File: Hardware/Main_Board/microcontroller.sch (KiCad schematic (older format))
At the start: 56 parts

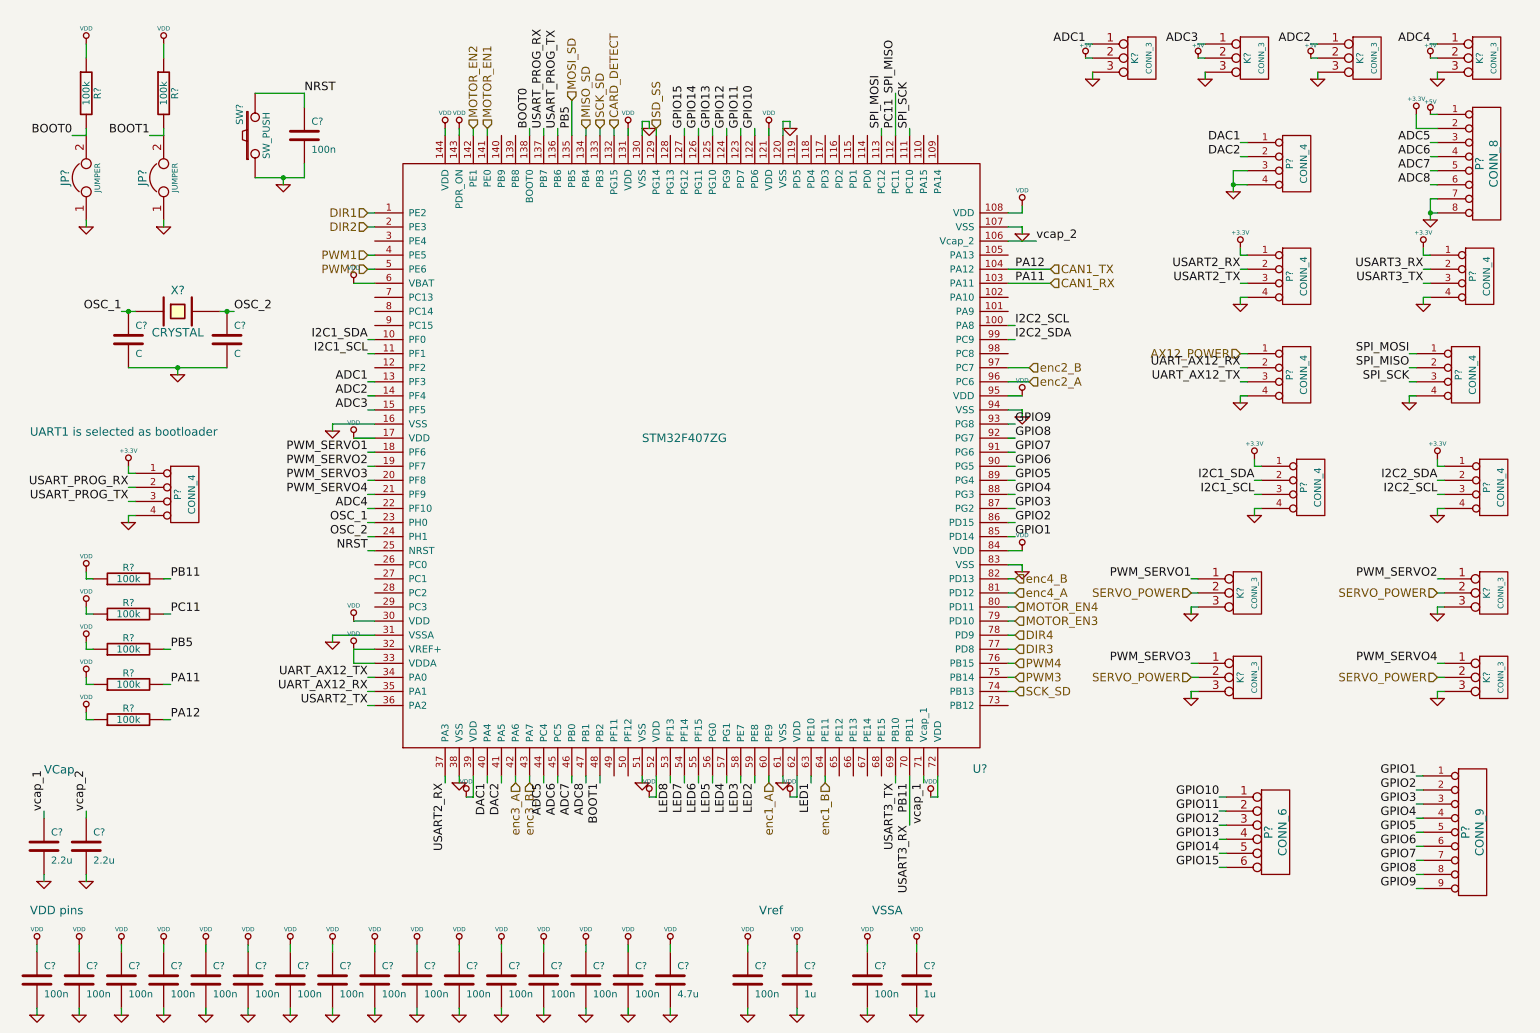
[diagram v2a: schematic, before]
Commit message: [HARDWARE] Add 4 ADC
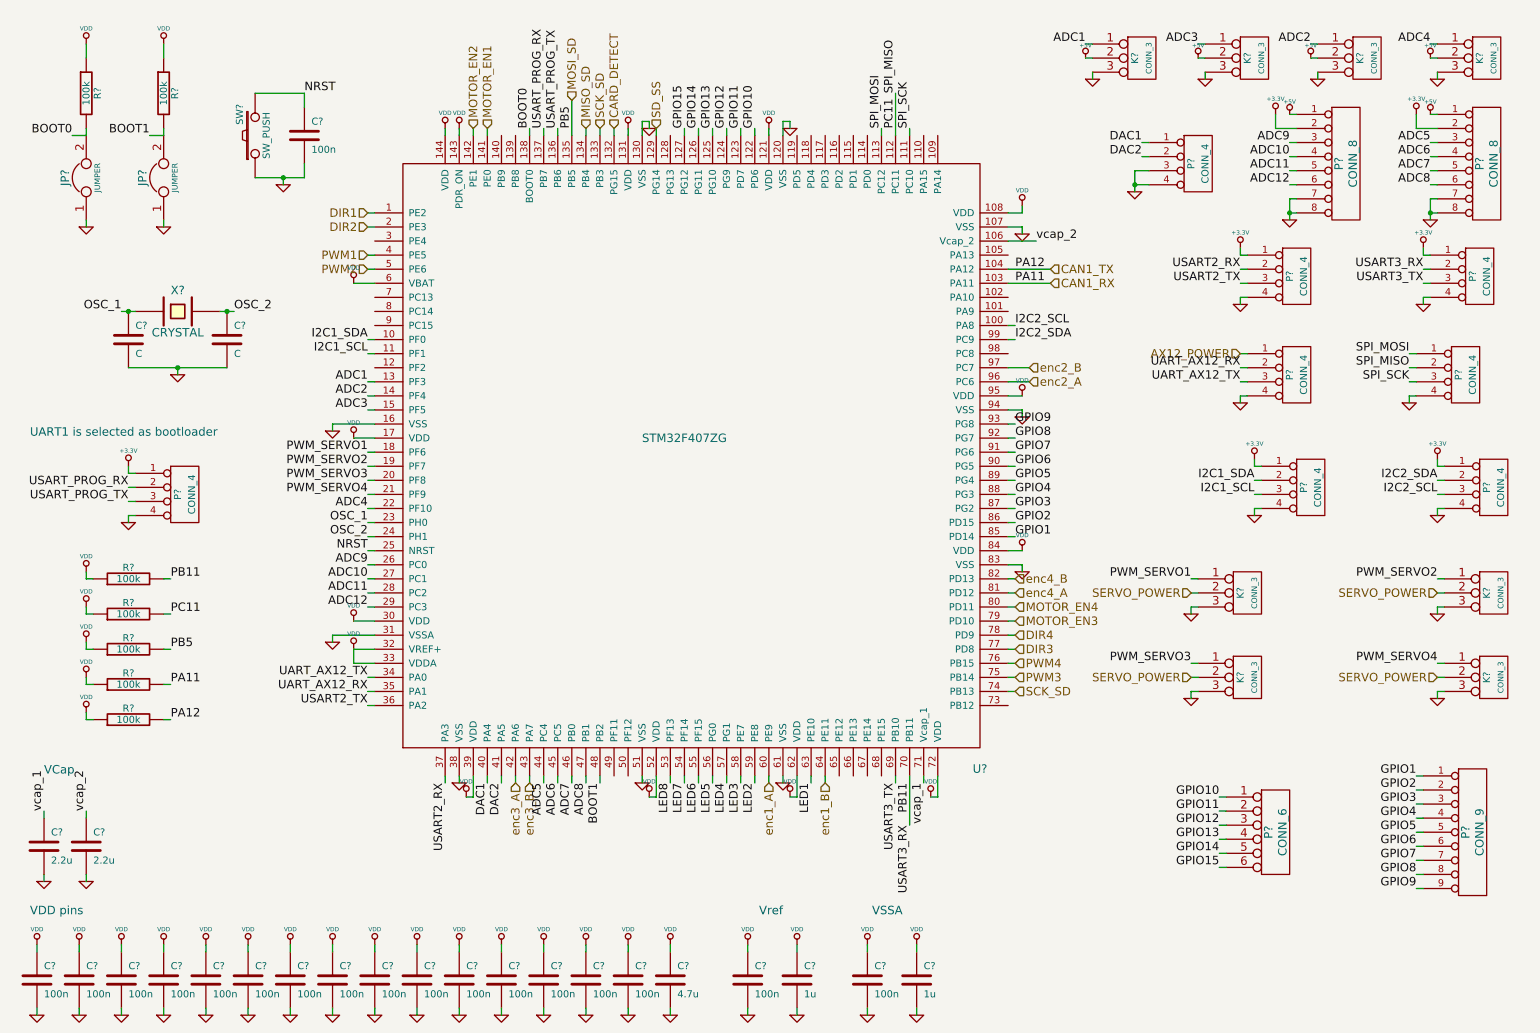
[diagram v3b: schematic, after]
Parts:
- added P?: CONN_8, symbol CONN_8
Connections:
- net +3.3V: now also P?.2 (P2)
- net +5V: now also P?.1 (P1)
- net GND: now also P?.7 (P7), P?.8 (P8)
- net ADC9: now reaches U?.26 (PC0)
- net ADC9: now also P?.3 (P3)
- net ADC10: now reaches U?.27 (PC1)
- net ADC10: now also P?.4 (P4)
- net ADC11: now reaches U?.28 (PC2)
- net ADC11: now also P?.5 (P5)
- net ADC12: now reaches U?.29 (PC3)
- net ADC12: now also P?.6 (P6)
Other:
- moved on the sheet: P?

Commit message: [HARDWARE] Finish motor interface and add SWD interface
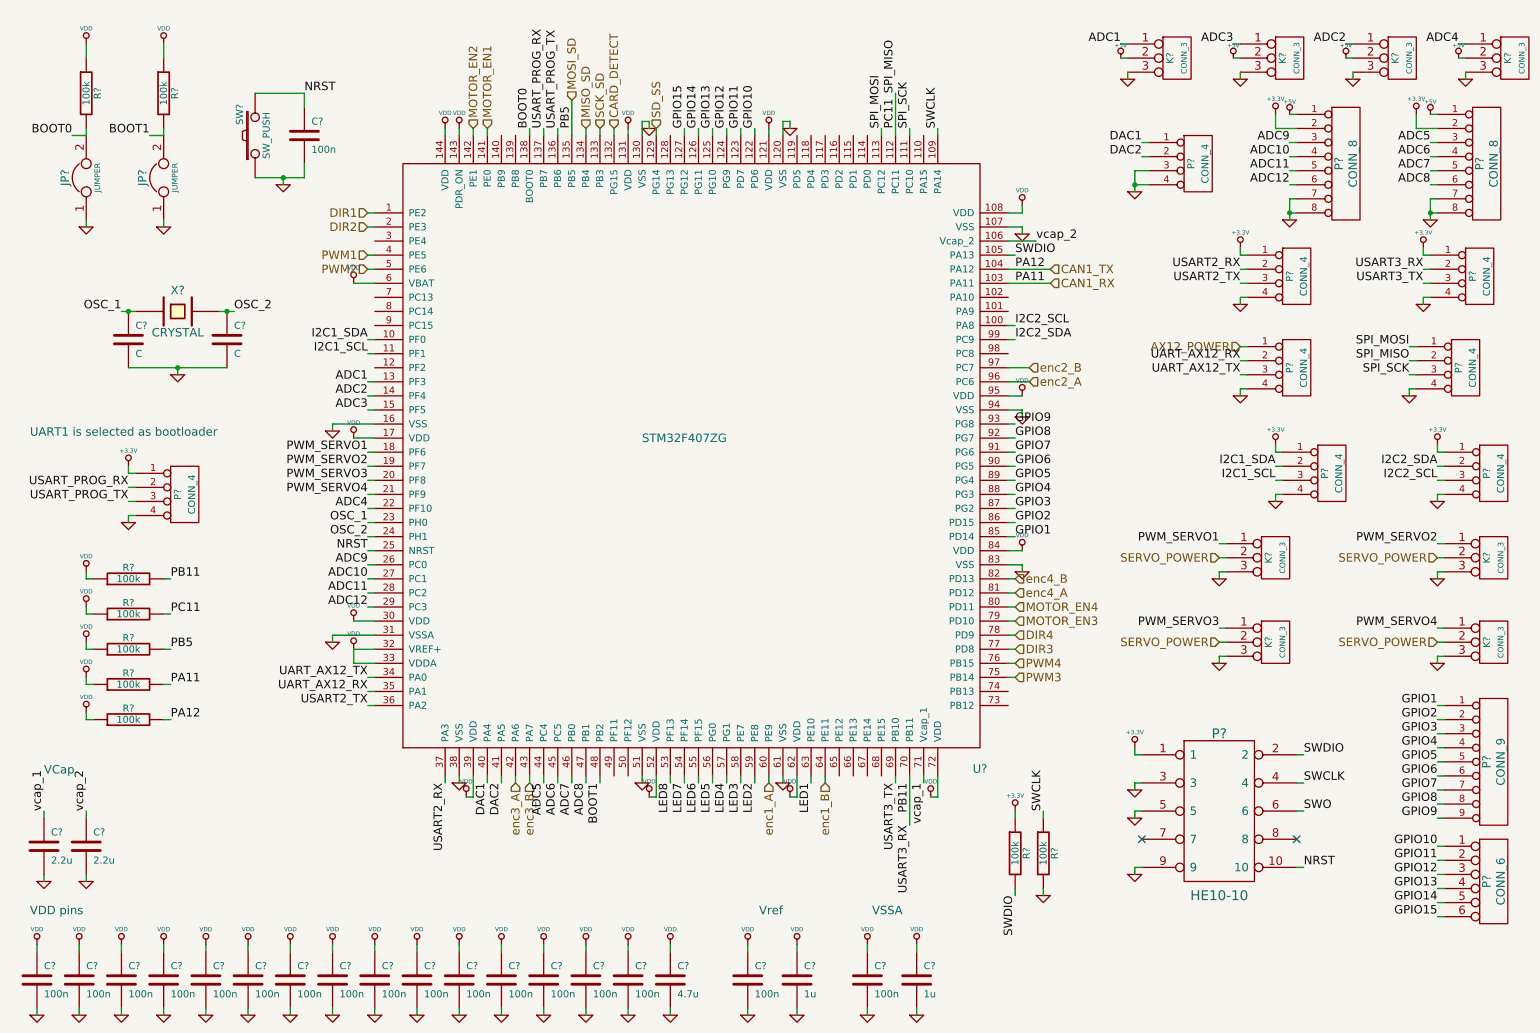
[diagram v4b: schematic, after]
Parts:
- added P?: HE10-10, symbol HE10-10
- added R? (x2): 100k, symbol R
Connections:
- net +3.3V: now also P?.1, R?.1
- net GND: now also P?.3, P?.5, P?.9, R?.2
- net NRST: now also P?.10
- net SCK_SD: no longer U?.74 (PB13)
- net SWDIO: now reaches U?.105 (PA13)
- net SWDIO: now also P?.2, R?.2
- net SWCLK: now reaches U?.109 (PA14)
- net SWCLK: now also P?.4, R?.1
- new net SWO: P?.6
- no-connect marks 0 -> 2
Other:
- moved on the sheet: K?, P?

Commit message: [HARDWARE] Complete the SWD design, remove two undrived motor interfaces
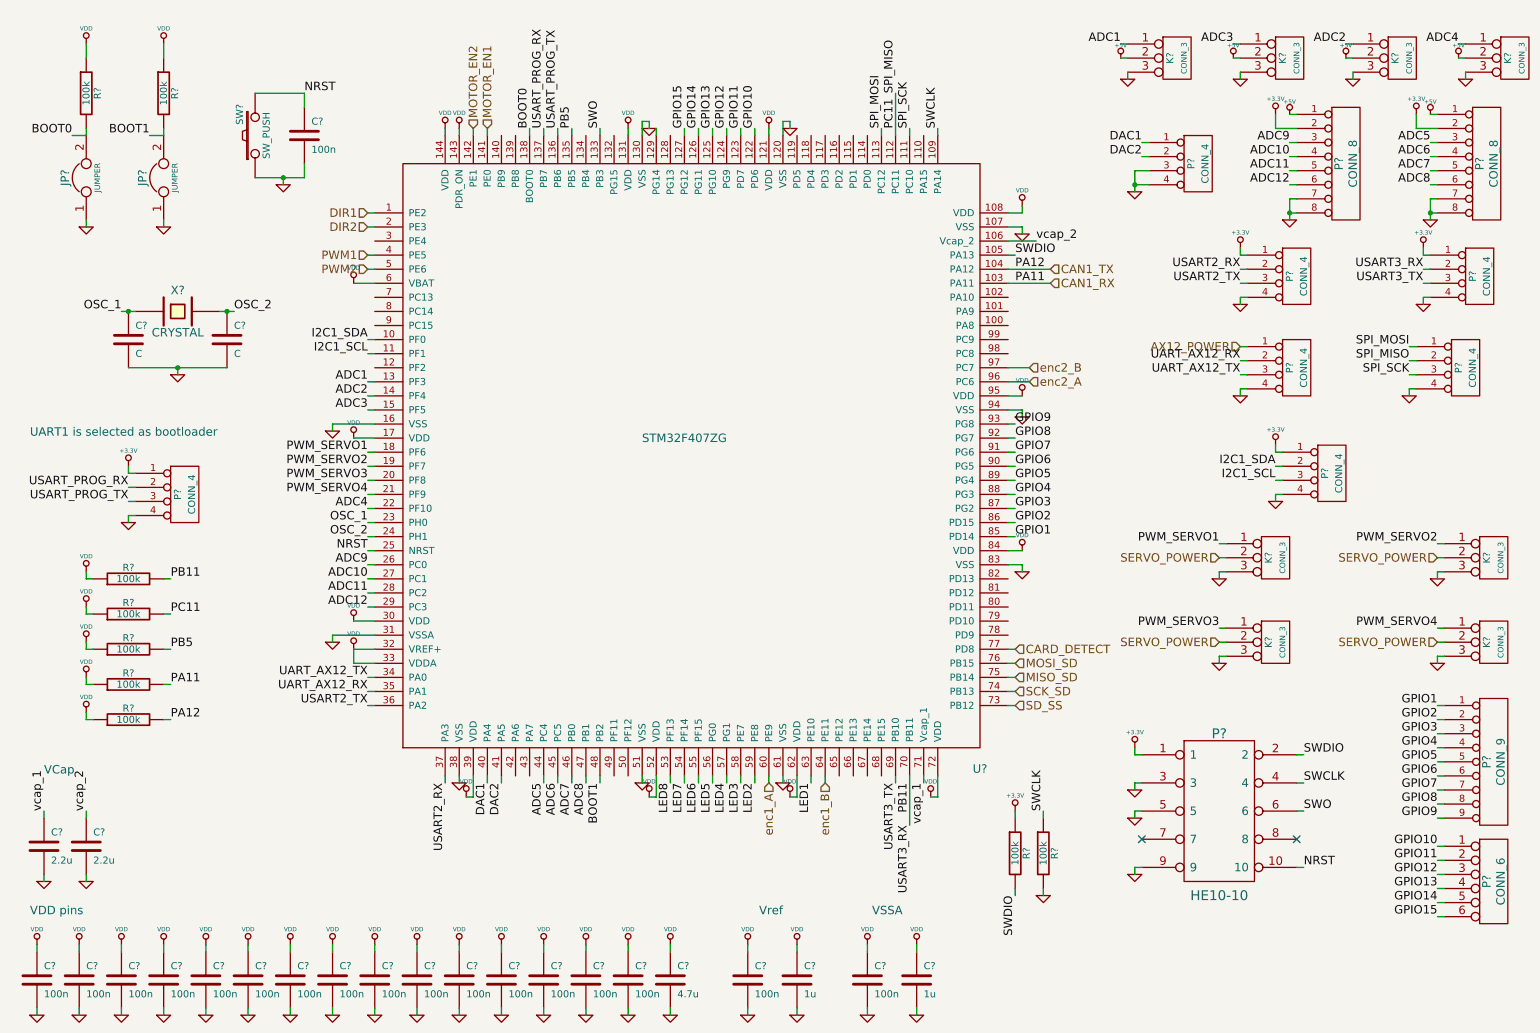
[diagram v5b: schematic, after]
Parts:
- removed P?: CONN_4, symbol CONN_4
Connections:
- net DIR3 is gone; now on net CARD_DETECT: U?.77 (PD8)
- net PWM3 is gone; now on net MISO_SD: U?.75 (PB14)
- net PWM4 is gone; now on net MOSI_SD: U?.76 (PB15)
- net CARD_DETECT: no longer U?.132 (PG15)
- net MISO_SD: no longer U?.134 (PB4)
- net MOSI_SD: no longer R?.2, U?.135 (PB5)
- net SCK_SD: now also U?.74 (PB13); no longer U?.133 (PB3)
- net SD_SS: now also U?.73 (PB12); no longer U?.129 (PG14)
- net SWO: now also U?.133 (PB3)
- net DIR4: no longer names the net of U?.78 (PD9)
- net I2C2_SCL: no longer names the net of U?.100 (PA8)
- net I2C2_SDA: no longer names the net of U?.99 (PC9)
- net MOTOR_EN3: no longer names the net of U?.79 (PD10)
- net MOTOR_EN4: no longer names the net of U?.80 (PD11)
- net enc3_A: no longer names the net of U?.42 (PA6)
- net enc3_B: no longer names the net of U?.43 (PA7)
- net enc4_A: no longer names the net of U?.81 (PD12)
- net enc4_B: no longer names the net of U?.82 (PD13)
- new net PB5: R?.2, U?.135 (PB5)

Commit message: [HARDWARE] Component association + schematic modifications
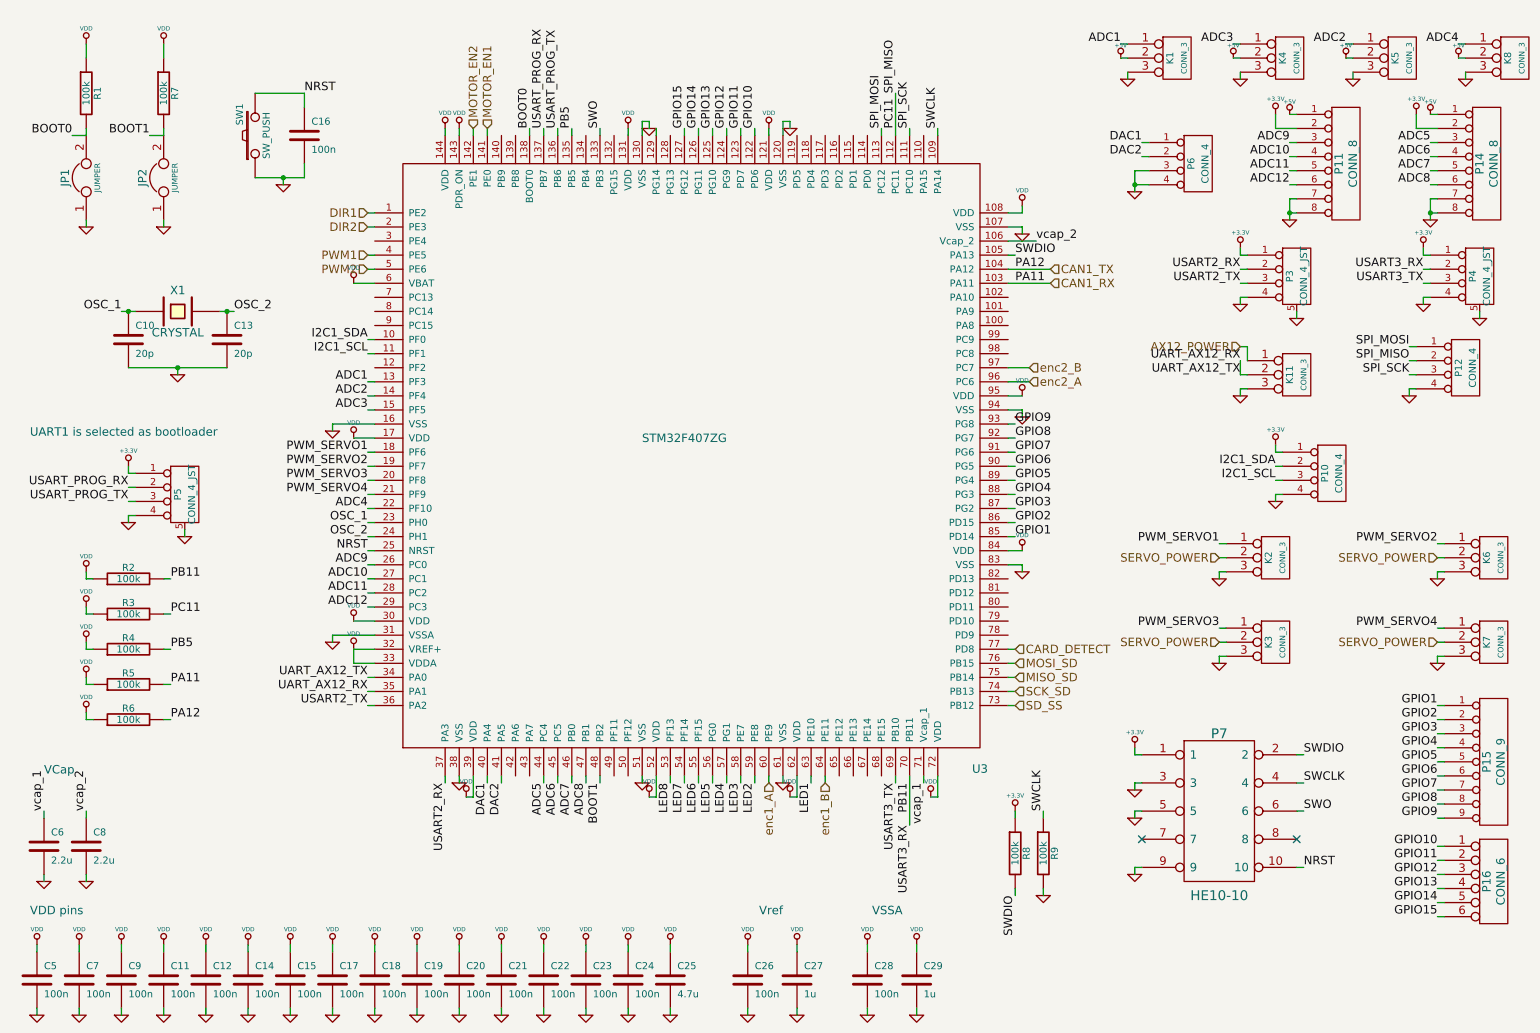
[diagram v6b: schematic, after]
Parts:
- removed P? (x4): CONN_4, symbol CONN_4
- added K11: CONN_3, symbol CONN_3
- added P3, P4, P5: CONN_4_JST, symbol CONN_4_JST
- C10, C13: renamed from C?; value C -> 20p
- gave numbers to parts that had none: 53
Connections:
- net UART_AX12_TX is gone; now on net UART_AX12_RX: U3.34 (PA0)
- net +3.3V: now also P3.1 (P1), P4.1 (P1), P5.1 (P1)
- net AX12_POWER: now also K11.1 (P1)
- net GND: now also K11.3 (P3), P3.4 (P4), P3.5 (Shield), P4.4 (P4), P4.5 (Shield), P5.4 (P4), P5.5 (Shield)
- net PB11: now also P4.2 (P2)
- net UART_AX12_RX: now also K11.2 (PM)
- net USART2_RX: now also P3.2 (P2)
- net USART2_TX: now also P3.3 (P3)
- net USART3_TX: now also P4.3 (P3)
- net USART_PROG_RX: now also P5.2 (P2)
- net USART_PROG_TX: now also P5.3 (P3)

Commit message: [HARDWARE] Update schematic and start routing
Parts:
- removed C23, C24, C28: 100n, symbol C
- removed C25: 4.7u, symbol C
- removed C29: 1u, symbol C
- removed P11: CONN_8, symbol CONN_8
- removed P16: CONN_6, symbol CONN_6
- added D10, D11, D12, D13, D14, D15, D16, D9: LED, symbol LED
- added R12, R13, R14, R15, R16, R17, R18, R19: 390, symbol R
- added R21, R22: 4.7k, symbol R
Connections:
- net GPIO10 is gone; now on net LED1: U3.122 (PD6)
- net GPIO11 is gone; now on net LED2: U3.123 (PD7)
- net GPIO12 is gone; now on net LED3: U3.124 (PG9)
- net GPIO13 is gone; now on net LED4: U3.125 (PG10)
- net GPIO14 is gone; now on net LED5: U3.126 (PG11)
- net GPIO15 is gone; now on net LED6: U3.127 (PG12)
- net +3.3V: now also R21.1, R22.1
- net CARD_DETECT: now also U3.68 (PE15); no longer U3.77 (PD8)
- net GND: now also D10.2 (K), D11.2 (K), D12.2 (K), D13.2 (K), D14.2 (K), D15.2 (K), D16.2 (K), D9.2 (K)
- net I2C1_SCL: now also R22.2
- net I2C1_SDA: now also R21.2
- net LED1: now also R12.1; no longer U3.63 (PE10)
- net LED2: now also R13.1; no longer U3.59 (PE8)
- net LED3: now also R14.1; no longer U3.58 (PE7)
- net LED4: now also R15.1; no longer U3.57 (PG1)
- net LED5: now also R16.1; no longer U3.56 (PG0)
- net LED6: now also R17.1; no longer U3.55 (PF15)
- net LED7: now also U3.128 (PG13), R18.1; no longer U3.54 (PF14)
- net LED8: now also U3.129 (PG14), R19.1; no longer U3.53 (PF13)
- net ADC10: no longer names the net of U3.27 (PC1)
- net ADC11: no longer names the net of U3.28 (PC2)
- net ADC12: no longer names the net of U3.29 (PC3)
- net ADC9: no longer names the net of U3.26 (PC0)
- new net: D9.1 (A), R12.2
- new net: D10.1 (A), R13.2
- new net: D12.1 (A), R15.2
- new net: D11.1 (A), R14.2
- new net: D15.1 (A), R18.2
- new net: D16.1 (A), R19.2
- new net: D14.1 (A), R17.2
- new net: D13.1 (A), R16.2
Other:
- note added: "SWD"
- note added: "Vref/Vssa"
- note removed: "VSSA"
- note removed: "Vref"

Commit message: [HARDWARE] Use JTAG + routing
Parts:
- added R23: 100k, symbol R
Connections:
- net +3.3V: now also R23.1
- net TDI: now reaches U3.110 (PA15)
- net TDI: now also P7.8, R8.2
- net SWCLK renamed TCLK
- net SWDIO renamed TMS
- net TMS: now also R23.2; no longer R8.2
- net SWO renamed TDO
- no-connect marks 2 -> 1
